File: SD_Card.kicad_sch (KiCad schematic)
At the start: 0 parts

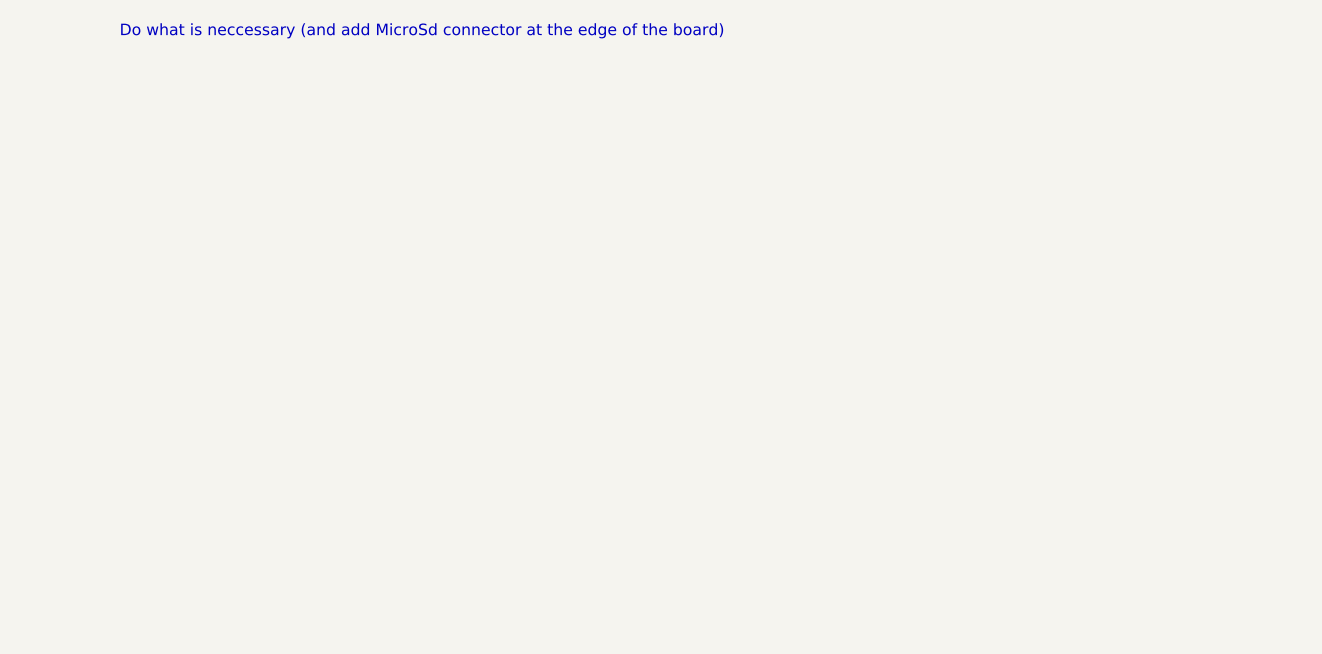
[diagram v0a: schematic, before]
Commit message: Latest changes (added SD , USB , CAN , RS485)
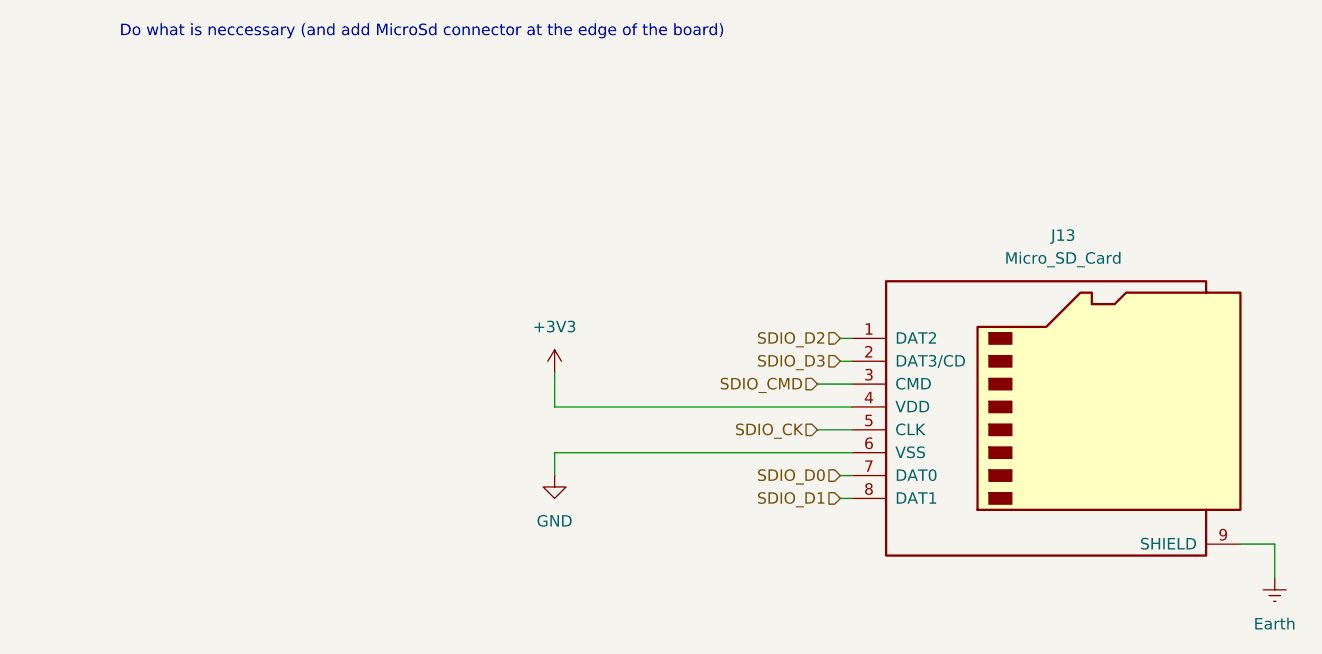
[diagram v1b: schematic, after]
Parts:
- added J13: Micro_SD_Card, symbol Connector:Micro_SD_Card
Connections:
- new net +3V3: J13.4 (VDD)
- new net Earth: J13.9 (SHIELD)
- new net GND: J13.6 (VSS)
- new net SDIO_CK: J13.5 (CLK)
- new net SDIO_CMD: J13.3 (CMD)
- new net SDIO_D0: J13.7 (DAT0)
- new net SDIO_D1: J13.8 (DAT1)
- new net SDIO_D2: J13.1 (DAT2)
- new net SDIO_D3: J13.2 (DAT3/CD)

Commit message: Schematic--Footprint link
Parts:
- J13: footprint (none) -> Connector_Card:microSD_HC_Molex_47219-2001
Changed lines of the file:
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@@
 			)
 		)
-		(property "Footprint" ""
+		(property "Footprint" "Connector_Card:microSD_HC_Molex_47219-2001"
 			(at 162.56 59.69 0)
 			(effects
